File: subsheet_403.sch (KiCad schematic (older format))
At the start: 44 parts, among them Q404 2N3904, Q405 2N3904, U403 MC1377_COLOR_TELEVISION_RGB_T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

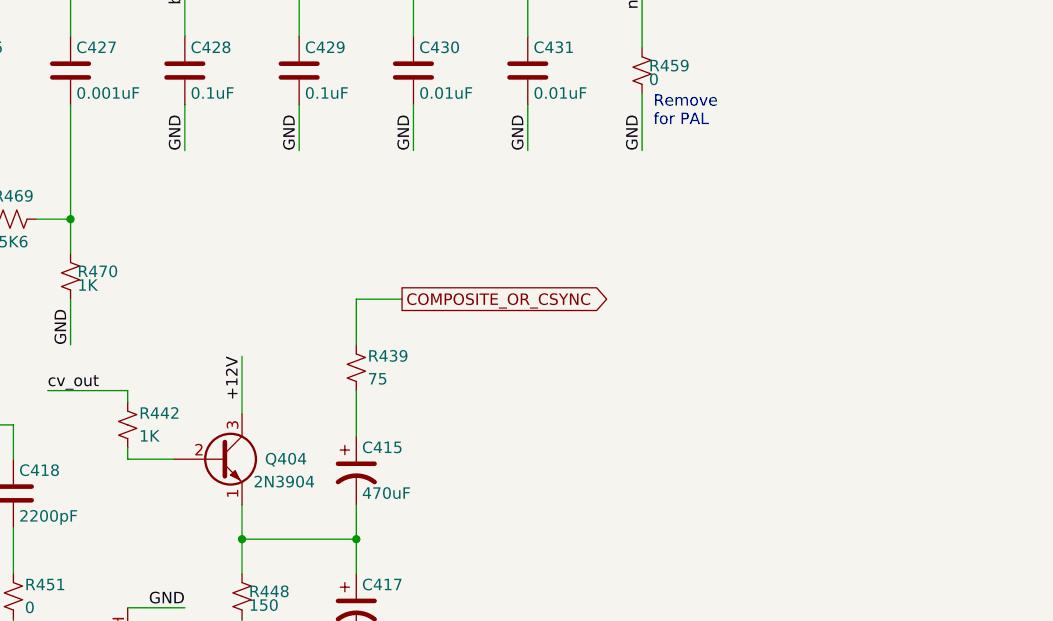
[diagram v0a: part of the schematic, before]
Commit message: [Schematics] reference the fact that C415 is reversed.
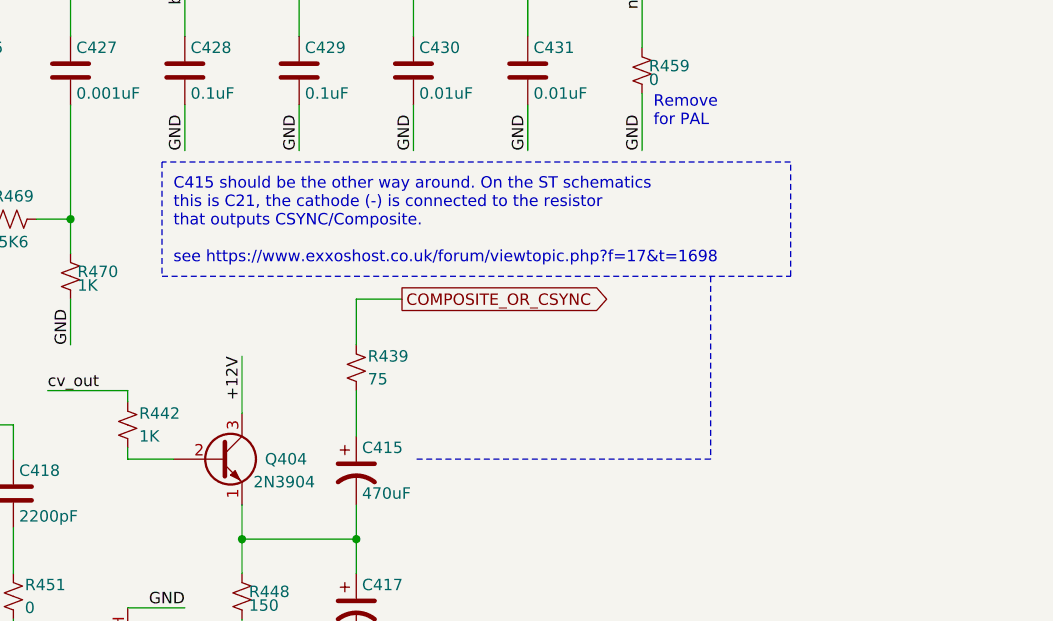
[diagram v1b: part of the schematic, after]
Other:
- note added: "C415 should be the other way around. On the ST schematics\nthis is C21, the cathode (-) is connected to the resistor\nthat outputs CSYNC/Composite.\n\nsee https://www.exxoshost.co.uk/forum/viewtopic.php?f=17&t=1698"
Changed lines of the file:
@@
 Wire Wire Line
 	4900 6400 4900 6450
+Text Notes 5100 5850 0    50   ~ 0
+C415 should be the other way around. On the ST schematics\nthis is C21, the cathode (-) is connected to the resistor\nthat outputs CSYNC/Composite.\n\nsee https://www.exxoshost.co.uk/forum/viewtopic.php?f=17&t=1698
+Wire Notes Line
+	7800 5400 5050 5400
+Wire Notes Line
+	5050 5400 5050 5900
+Wire Notes Line
+	5050 5900 7800 5900
+Wire Notes Line
+	7800 5900 7800 5400
+Wire Notes Line
+	7450 5900 7450 6700
+Wire Notes Line
+	7450 6700 6150 6700
 $EndSCHEMATC
